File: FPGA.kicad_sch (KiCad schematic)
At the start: 1 part, among them U3 XC7A100T-FTG256

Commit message: Added on chip osillator to FPGA
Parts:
- added C52, C53: 100n, symbol Device:C
- added R10: 2.4k, symbol Device:R
- added R11, R12: 4.7k, symbol Device:R
- added U5: ~, symbol GuitarZero:SpiFlashPlaceholder
- added U6: ~, symbol GuitarZero:oscilator
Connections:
- net +3.3V: now also C52.1, C53.1, R10.2, R11.2, R12.2, U5.8 (VCC), U6.1 (E/D), U6.4 (VCC)
- net GND: now also C52.2, C53.2, U5.4 (VSS), U6.2 (GND)
- net at U3.J13 (IO_L1P_T0_D00_MOSI_14): now also U5.5 (DQ0)
- net at U3.J14 (IO_L1N_T0_D01_DIN_14): now also U5.2 (DQ1)
- net at U3.K15 (IO_L2P_T0_D02_14): now also U5.3 (W#/Vpp/DQ2)
- net at U3.K16 (IO_L2N_T0_D03_14): now also R12.1, U5.7 (HOLD#/DQ3)
- net at U3.N11 (IO_L13P_T2_MRCC_14): now also U6.3 (OUTPUT)
- net at U3.E8 (CCLK_0): now also U5.6 (C)
- new net: R10.1, U5.1 (S#)
- no-connect marks 0 -> 70
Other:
- note added: "FPGA JTAG Debug Connectors"
- note added: "Oscilator"
- note added: "Power Connections"
- note added: "Spi Flash Memory"
- moved on the sheet: U3A, U3B, U3C

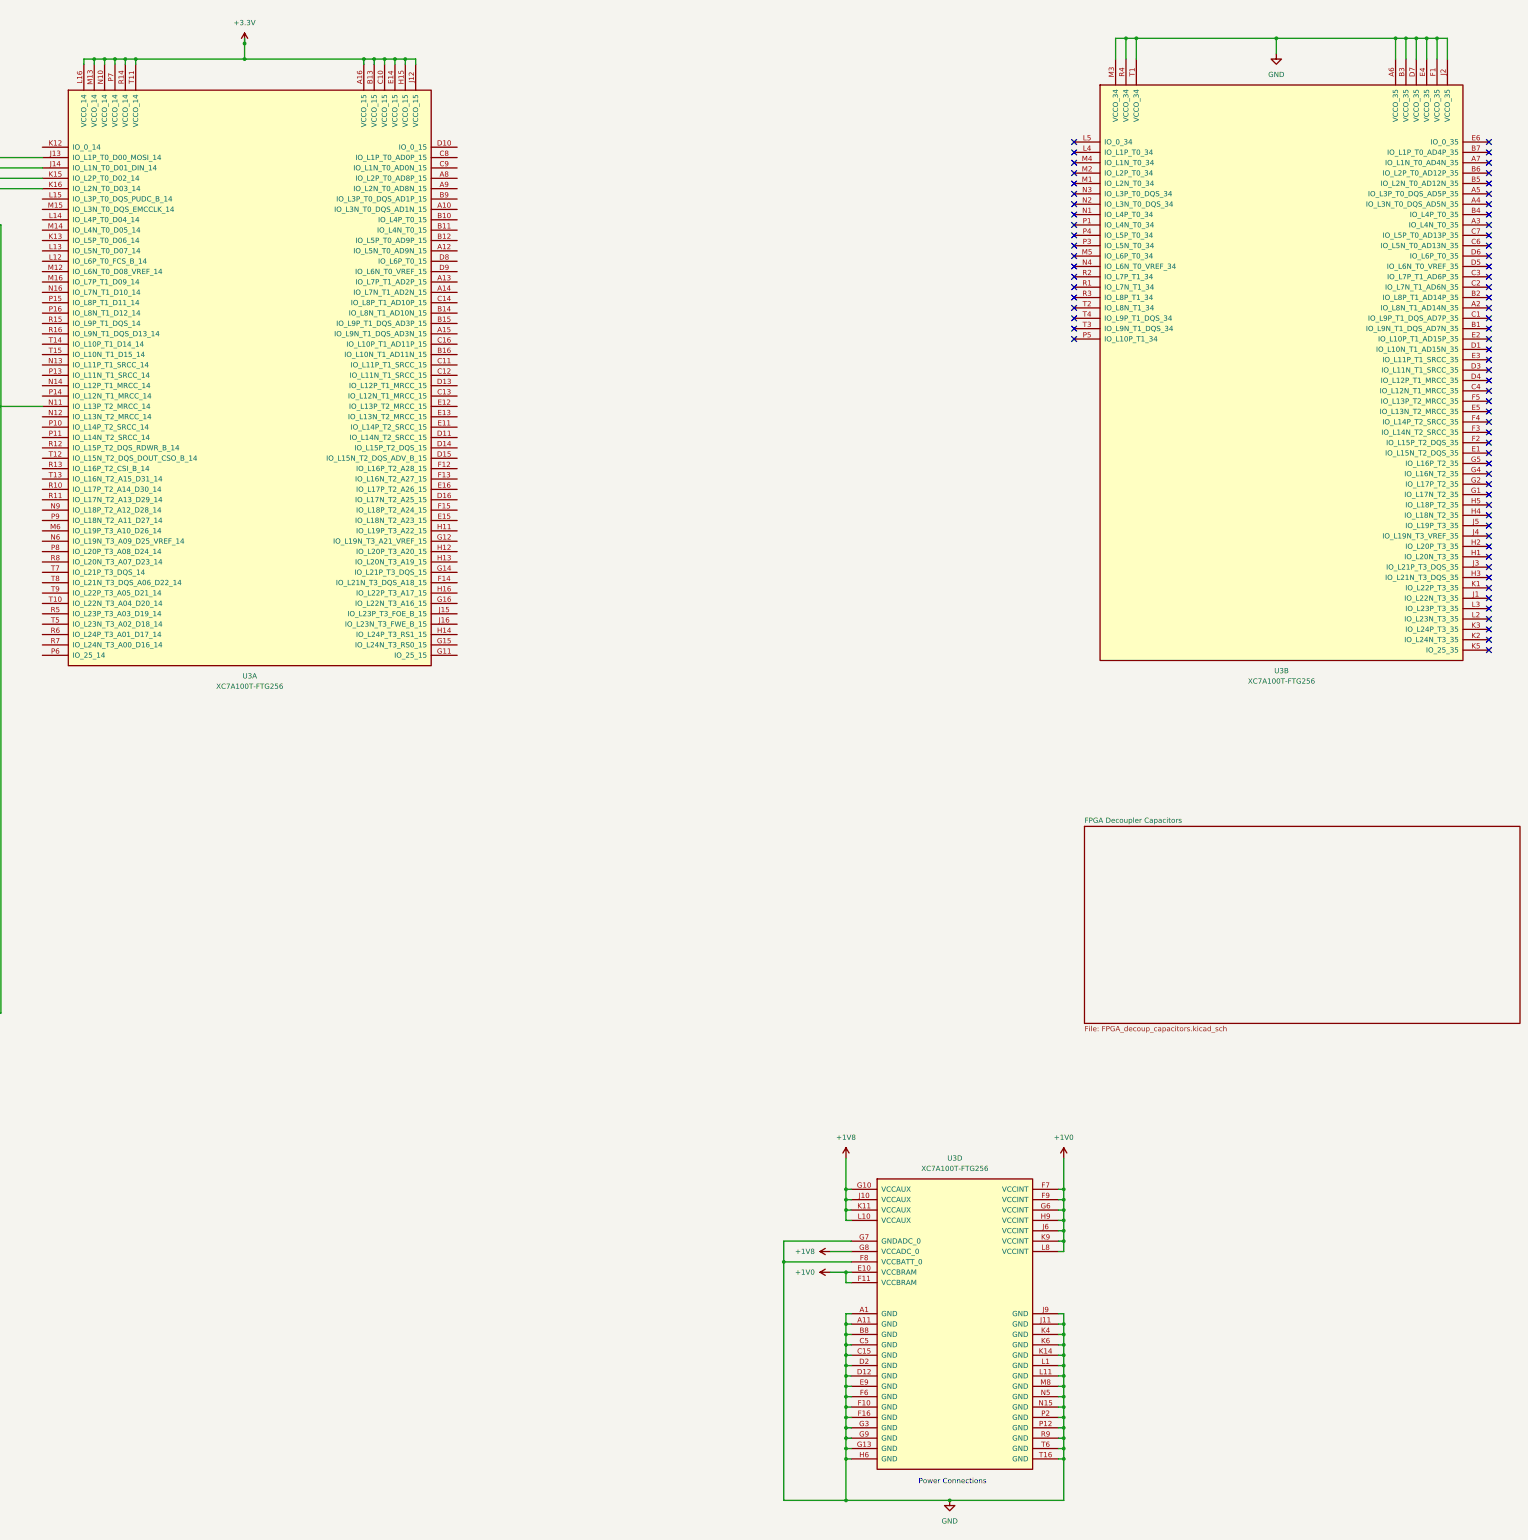
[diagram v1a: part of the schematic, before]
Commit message: Disconnected unused I/O bank in FPGA
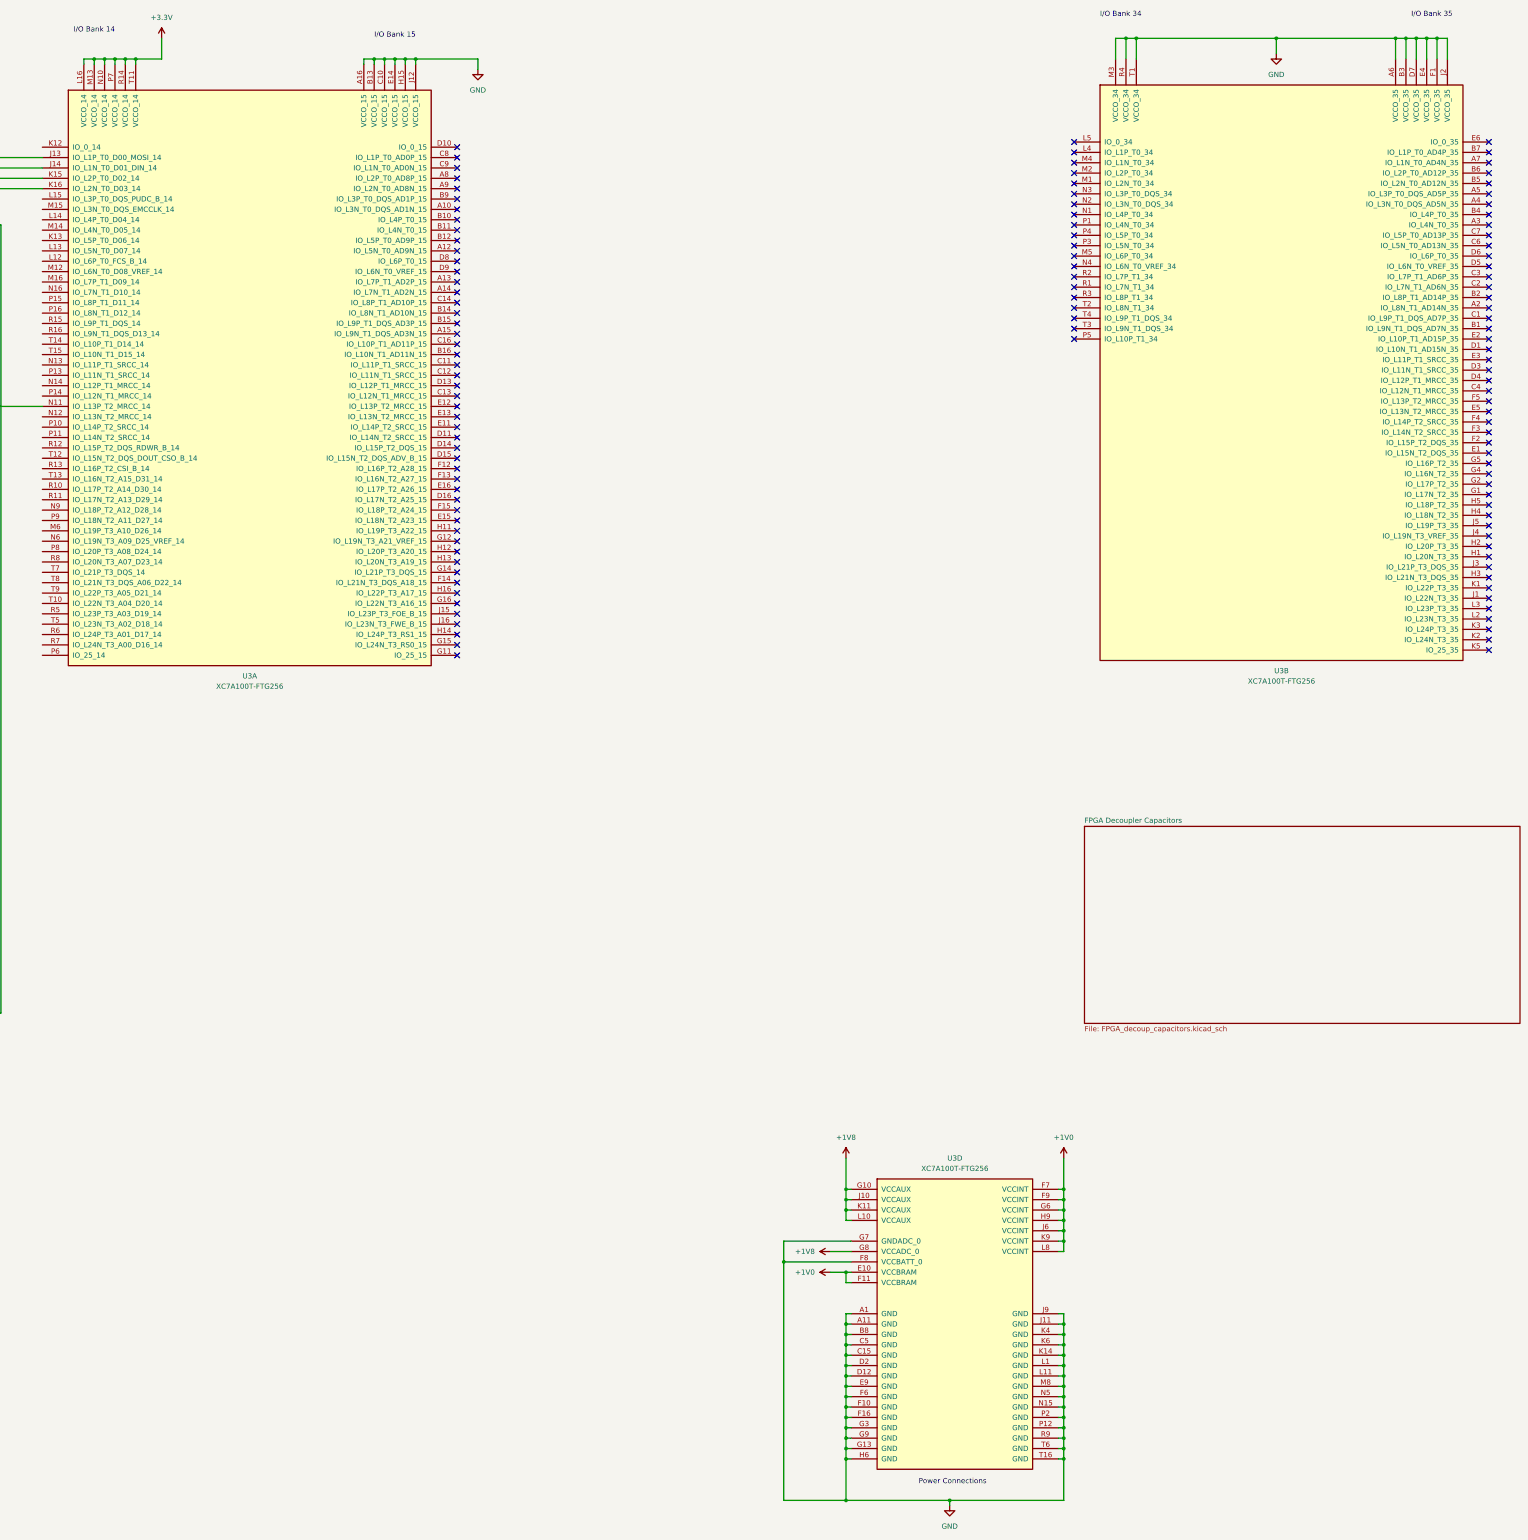
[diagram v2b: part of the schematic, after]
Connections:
- net +3.3V: no longer U3.A16 (VCCO_15), U3.B13 (VCCO_15), U3.C10 (VCCO_15), U3.E14 (VCCO_15), U3.H15 (VCCO_15), U3.J12 (VCCO_15)
- net GND: now also U3.A16 (VCCO_15), U3.B13 (VCCO_15), U3.C10 (VCCO_15), U3.E14 (VCCO_15), U3.H15 (VCCO_15), U3.J12 (VCCO_15)
- no-connect marks 70 -> 120
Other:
- note added: "I/O Bank 14"
- note added: "I/O Bank 15"
- note added: "I/O Bank 34"
- note added: "I/O Bank 35"
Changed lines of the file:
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@@
   (junction (at 265.43 35.56) (diameter 0) (color 0 0 0 0)
   )
-  (junction (at 262.89 35.56) (diameter 0) (color 0 0 0 0)
-  )
   (junction (at 270.51 35.56) (diameter 0) (color 0 0 0 0)
   )
@@
   (junction (at 381 350.52) (diameter 0) (color 0 0 0 0)
   )
-  (junction (at 233.68 35.56) (diameter 0) (color 0 0 0 0)
-  )
   (junction (at 196.85 35.56) (diameter 0) (color 0 0 0 0)
   )
@@
   (junction (at 381 317.5) (diameter 0) (color 0 0 0 0)
   )
+  (junction (at 275.59 35.56) (diameter 0) (color 0 0 0 0)
+  )
   (junction (at 201.93 35.56) (diameter 0) (color 0 0 0 0)
   )
@@
   (junction (at 381 353.06) (diameter 0) (color 0 0 0 0)
   )
-  (junction (at 233.68 31.75) (diameter 0) (color 0 0 0 0)
-  )
   (junction (at 381 347.98) (diameter 0) (color 0 0 0 0)
   )
@@
   (junction (at 434.34 375.92) (diameter 0) (color 0 0 0 0)
   )
+  (no_connect (at 285.75 128.27))
   (no_connect (at 436.88 81.28))
   (no_connect (at 436.88 66.04))
@@
   (no_connect (at 538.48 96.52))
   (no_connect (at 436.88 101.6))
+  (no_connect (at 285.75 82.55))
+  (no_connect (at 285.75 118.11))
   (no_connect (at 538.48 124.46))
   (no_connect (at 538.48 127))
+  (no_connect (at 285.75 166.37))
   (no_connect (at 538.48 180.34))
   (no_connect (at 538.48 73.66))
   (no_connect (at 538.48 55.88))
   (no_connect (at 538.48 152.4))
+  (no_connect (at 285.75 80.01))
   (no_connect (at 436.88 60.96))
+  (no_connect (at 285.75 171.45))
   (no_connect (at 538.48 60.96))
   (no_connect (at 538.48 116.84))
   (no_connect (at 538.48 114.3))
+  (no_connect (at 285.75 143.51))
+  (no_connect (at 285.75 92.71))
   (no_connect (at 436.88 76.2))
   (no_connect (at 538.48 71.12))
@@
   (no_connect (at 436.88 58.42))
   (no_connect (at 538.48 170.18))
+  (no_connect (at 285.75 110.49))
+  (no_connect (at 285.75 151.13))
   (no_connect (at 436.88 63.5))
+  (no_connect (at 285.75 179.07))
   (no_connect (at 538.48 83.82))
+  (no_connect (at 285.75 62.23))
   (no_connect (at 436.88 73.66))
   (no_connect (at 538.48 167.64))
+  (no_connect (at 285.75 133.35))
   (no_connect (at 538.48 157.48))
+  (no_connect (at 285.75 173.99))
+  (no_connect (at 285.75 74.93))
+  (no_connect (at 285.75 161.29))
   (no_connect (at 538.48 106.68))
   (no_connect (at 538.48 104.14))
   (no_connect (at 538.48 137.16))
+  (no_connect (at 285.75 163.83))
+  (no_connect (at 285.75 130.81))
   (no_connect (at 538.48 93.98))
+  (no_connect (at 285.75 105.41))
+  (no_connect (at 285.75 135.89))
   (no_connect (at 538.48 109.22))
   (no_connect (at 538.48 68.58))
+  (no_connect (at 285.75 97.79))
   (no_connect (at 436.88 88.9))
+  (no_connect (at 285.75 140.97))
+  (no_connect (at 285.75 90.17))
   (no_connect (at 538.48 175.26))
   (no_connect (at 436.88 86.36))
   (no_connect (at 436.88 78.74))
   (no_connect (at 538.48 154.94))
+  (no_connect (at 285.75 156.21))
   (no_connect (at 436.88 71.12))
+  (no_connect (at 285.75 125.73))
   (no_connect (at 538.48 165.1))
+  (no_connect (at 285.75 59.69))
+  (no_connect (at 285.75 67.31))
+  (no_connect (at 285.75 123.19))
+  (no_connect (at 285.75 158.75))
   (no_connect (at 538.48 134.62))
+  (no_connect (at 285.75 176.53))
   (no_connect (at 436.88 104.14))
+  (no_connect (at 285.75 102.87))
+  (no_connect (at 285.75 77.47))
+  (no_connect (at 285.75 87.63))
   (no_connect (at 538.48 88.9))
+  (no_connect (at 285.75 95.25))
   (no_connect (at 538.48 142.24))
   (no_connect (at 538.48 78.74))
+  (no_connect (at 285.75 100.33))
+  (no_connect (at 285.75 148.59))
   (no_connect (at 538.48 111.76))
   (no_connect (at 538.48 129.54))
+  (no_connect (at 285.75 57.15))
   (no_connect (at 538.48 160.02))
   (no_connect (at 538.48 66.04))
@@
   (no_connect (at 538.48 147.32))
   (no_connect (at 436.88 68.58))
+  (no_connect (at 285.75 107.95))
+  (no_connect (at 285.75 168.91))
+  (no_connect (at 285.75 120.65))
   (no_connect (at 538.48 91.44))
   (no_connect (at 436.88 99.06))
+  (no_connect (at 285.75 153.67))
+  (no_connect (at 285.75 72.39))
   (no_connect (at 538.48 172.72))
   (no_connect (at 538.48 121.92))
+  (no_connect (at 285.75 64.77))
   (no_connect (at 538.48 144.78))
+  (no_connect (at 285.75 113.03))
   (no_connect (at 538.48 149.86))
   (no_connect (at 538.48 63.5))
+  (no_connect (at 285.75 69.85))
   (no_connect (at 538.48 132.08))
+  (no_connect (at 285.75 146.05))
+  (no_connect (at 285.75 115.57))
   (no_connect (at 538.48 101.6))
   (no_connect (at 538.48 139.7))
@@
   (no_connect (at 436.88 83.82))
   (no_connect (at 436.88 96.52))
+  (no_connect (at 285.75 181.61))
   (no_connect (at 538.48 76.2))
+  (no_connect (at 285.75 138.43))
   (no_connect (at 436.88 93.98))
+  (no_connect (at 285.75 85.09))
   (wire (pts (xy 152.4 104.14) (xy 152.4 105.41))
     (stroke (width 0) (type default))
@@
     (stroke (width 0) (type default))
   )
-  (wire (pts (xy 233.68 35.56) (xy 262.89 35.56))
-    (stroke (width 0) (type default))
-  )
   (wire (pts (xy 62.23 64.77) (xy 184.15 64.77))
     (stroke (width 0) (type default))
@@
     (stroke (width 0) (type default))
   )
+  (wire (pts (xy 406.4 389.89) (xy 406.4 388.62))
+    (stroke (width 0) (type default))
+  )
   (wire (pts (xy 486.41 30.48) (xy 515.62 30.48))
     (stroke (width 0) (type default))
@@
     (stroke (width 0) (type default))
   )
+  (wire (pts (xy 275.59 35.56) (xy 290.83 35.56))
+    (stroke (width 0) (type default))
+  )
   (wire (pts (xy 152.4 104.14) (xy 161.29 104.14))
     (stroke (width 0) (type default))
@@
     (stroke (width 0) (type default))
   )
+  (wire (pts (xy 290.83 35.56) (xy 290.83 38.1))
+    (stroke (width 0) (type default))
+  )
   (wire (pts (xy 194.31 35.56) (xy 194.31 36.83))
     (stroke (width 0) (type default))
@@
     (stroke (width 0) (type default))
   )
-  (wire (pts (xy 233.68 30.48) (xy 233.68 31.75))
+  (wire (pts (xy 213.36 30.48) (xy 213.36 35.56))
     (stroke (width 0) (type default))
   )
@@
     (stroke (width 0) (type default))
   )
-  (wire (pts (xy 207.01 35.56) (xy 233.68 35.56))
+  (wire (pts (xy 207.01 35.56) (xy 213.36 35.56))
     (stroke (width 0) (type default))
   )
@@
   )
   (wire (pts (xy 381 350.52) (xy 381 353.06))
-    (stroke (width 0) (type default))
-  )
-  (wire (pts (xy 233.68 35.56) (xy 233.68 31.75))
     (stroke (width 0) (type default))
   )
@@
     (effects (font (size 1.27 1.27)) (justify left bottom))
   )
+  (text "I/O Bank 35" (at 519.43 25.4 0)
+    (effects (font (size 1.27 1.27)) (justify left bottom))
+  )
+  (text "I/O Bank 34" (at 443.23 25.4 0)
+    (effects (font (size 1.27 1.27)) (justify left bottom))
+  )
+  (text "I/O Bank 15" (at 265.43 30.48 0)
+    (effects (font (size 1.27 1.27)) (justify left bottom))
+  )
   (text "Power Connections" (at 398.78 384.81 0)
     (effects (font (size 1.27 1.27)) (justify left bottom))
   )
   (text "Oscilator" (at 137.16 127 0)
+    (effects (font (size 1.27 1.27)) (justify left bottom))
+  )
+  (text "I/O Bank 14" (at 191.77 29.21 0)
     (effects (font (size 1.27 1.27)) (justify left bottom))
   )
@@
         (path "/fba50eda-8593-4456-af98-ff56fd418a76/7788bc9b-1e55-4835-b7d3-ea790efb8c61"
           (reference "#PWR022") (unit 1)
+        )
+      )
+    )
+  )
+  (symbol (lib_id "power:GND") (at 290.83 38.1 0) (unit 1)
+    (in_bom yes) (on_board yes) (dnp no) (fields_autoplaced)
+    (property "Reference" "#PWR028" (at 290.83 44.45 0)
+      (effects (font (size 1.27 1.27)) hide)
+    )
+    (property "Value" "GND" (at 290.83 43.18 0)
+      (effects (font (size 1.27 1.27)))
+    )
+    (property "Footprint" "" (at 290.83 38.1 0)
+      (effects (font (size 1.27 1.27)) hide)
+    )
+    (property "Datasheet" "" (at 290.83 38.1 0)
+      (effects (font (size 1.27 1.27)) hide)
+    )
+    (pin "1")
+    (instances
+      (project "GuitarZero"
+        (path "/fba50eda-8593-4456-af98-ff56fd418a76/7788bc9b-1e55-4835-b7d3-ea790efb8c61"
+          (reference "#PWR028") (unit 1)
         )
       )
@@
     )
   )
-  (symbol (lib_id "power:+3.3V") (at 233.68 31.75 0) (unit 1)
+  (symbol (lib_id "power:+3.3V") (at 213.36 30.48 0) (unit 1)
     (in_bom yes) (on_board yes) (dnp no) (fields_autoplaced)
-    (property "Reference" "#PWR021" (at 233.68 35.56 0)
-      (effects (font (size 1.27 1.27)) hide)
-    )
-    (property "Value" "+3.3V" (at 233.68 26.67 0)
-      (effects (font (size 1.27 1.27)))
-    )
-    (property "Footprint" "" (at 233.68 31.75 0)
-      (effects (font (size 1.27 1.27)) hide)
-    )
-    (property "Datasheet" "" (at 233.68 31.75 0)
+    (property "Reference" "#PWR021" (at 213.36 34.29 0)
+      (effects (font (size 1.27 1.27)) hide)
+    )
+    (property "Value" "+3.3V" (at 213.36 25.4 0)
+      (effects (font (size 1.27 1.27)))
+    )
+    (property "Footprint" "" (at 213.36 30.48 0)
+      (effects (font (size 1.27 1.27)) hide)
+    )
+    (property "Datasheet" "" (at 213.36 30.48 0)
       (effects (font (size 1.27 1.27)) hide)
     )
@@
     )
   )
-  (symbol (lib_id "power:GND") (at 406.4 388.62 0) (unit 1)
+  (symbol (lib_id "power:GND") (at 406.4 389.89 0) (unit 1)
     (in_bom yes) (on_board yes) (dnp no) (fields_autoplaced)
-    (property "Reference" "#PWR016" (at 406.4 394.97 0)
-      (effects (font (size 1.27 1.27)) hide)
-    )
-    (property "Value" "GND" (at 406.4 393.7 0)
-      (effects (font (size 1.27 1.27)))
-    )
-    (property "Footprint" "" (at 406.4 388.62 0)
-      (effects (font (size 1.27 1.27)) hide)
-    )
-    (property "Datasheet" "" (at 406.4 388.62 0)
-      (effects (font (size 1.27 1.27)) hide)
-    )
+    (property "Reference" "#PWR016" (at 406.4 396.24 0)
+      (effects (font (size 1.27 1.27)) hide)
+    )
+    (property "Value" "GND" (at 406.4 394.97 0)
+      (effects (font (size 1.27 1.27)))
+    )
+    (property "Footprint" "" (at 406.4 389.89 0)
+      (effects (font (size 1.27 1.27)) hide)
+    )
+    (property "Datasheet" "" (at 406.4 389.89 0)
+      (effects (font (size 1.27 1.27)) hide)
+    )

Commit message: Resized FPGA file down to A3 from A2 to improve readability
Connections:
- net GND is gone; now on net +3.3V: C52.2, C53.2, U3.A1 (GND), U3.A11 (GND), U3.A16 (VCCO_15), U3.A6 (VCCO_35), U3.B13 (VCCO_15), U3.B3 (VCCO_35), U3.B8 (GND), U3.C10 (VCCO_15), U3.C15 (GND), U3.C5 (GND), U3.D12 (GND), U3.D2 (GND), U3.D7 (VCCO_35), U3.E14 (VCCO_15), U3.E4 (VCCO_35), U3.E9 (GND), U3.F1 (VCCO_35), U3.F10 (GND), U3.F16 (GND), U3.F6 (GND), U3.F8 (VCCBATT_0), U3.G13 (GND), U3.G3 (GND), U3.G7 (GNDADC_0), U3.G9 (GND), U3.H15 (VCCO_15), U3.H6 (GND), U3.J11 (GND), U3.J12 (VCCO_15), U3.J2 (VCCO_35), U3.J9 (GND), U3.K14 (GND), U3.K4 (GND), U3.K6 (GND), U3.L1 (GND), U3.L11 (GND), U3.M3 (VCCO_34), U3.M8 (GND), U3.N15 (GND), U3.N5 (GND), U3.P12 (GND), U3.P2 (GND), U3.R4 (VCCO_34), U3.R9 (GND), U3.T1 (VCCO_34), U3.T16 (GND), U3.T6 (GND), U5.4 (VSS), U6.2 (GND)
- net +3.3V: now also U3.L15 (IO_L3P_T0_DQS_PUDC_B_14), U3.N11 (IO_L13P_T2_MRCC_14), U6.3 (OUTPUT)
- net at U3.K15 (IO_L2P_T0_D02_14), U5.3 (W#/Vpp/DQ2): now also R11.1
- net at U3.L12 (IO_L6P_T0_FCS_B_14): now also R10.1, U5.1 (S#)
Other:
- moved on the sheet: C52, R10, R11, R12, U3A, U3B, U3C, U3D, U5
